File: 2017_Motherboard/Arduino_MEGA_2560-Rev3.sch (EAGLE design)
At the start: 93 parts, among them IC1 NCP1117ST50T3G, IC2 FT232RL, IC3 ATMEGA2560-16AU, IC4 MAX4312ESE, IC5 MAX3468CPA, IC7 LMV358IDGKR, X1 POWERSUPPLY_DC21MMX, Y1 CSTCE16M0V53-R0 16MHZ

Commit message: Updated part names
minor changes
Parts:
- renumbered J9 to ESC_PWM_GND
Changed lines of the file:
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@@
 <part name="J7" library="SparkFun-Connectors" deviceset="M02" device="PTH"/>
 <part name="J8" library="SparkFun-Connectors" deviceset="M02" device="PTH"/>
-<part name="J9" library="SparkFun-Connectors" deviceset="M06" device="LONGPADS"/>
+<part name="ESC_PWM_GND" library="SparkFun-Connectors" deviceset="M06" device="LONGPADS"/>
 <part name="J10" library="SparkFun-Connectors" deviceset="M02" device="PTH"/>
 <part name="J11" library="SparkFun-Connectors" deviceset="M02" device="PTH"/>
@@
 <instance part="J7" gate="G$1" x="337.82" y="114.3" rot="R180"/>
 <instance part="J8" gate="G$1" x="337.82" y="127" rot="R180"/>
-<instance part="J9" gate="G$1" x="261.62" y="38.1" rot="MR0"/>
+<instance part="ESC_PWM_GND" gate="G$1" x="261.62" y="38.1" rot="MR0"/>
 <instance part="J10" gate="G$1" x="152.4" y="-76.2" rot="R180"/>
 <instance part="J11" gate="G$1" x="104.14" y="-48.26" rot="R180"/>
@@
 </segment>
 <segment>
-<pinref part="J9" gate="G$1" pin="6"/>
+<pinref part="ESC_PWM_GND" gate="G$1" pin="6"/>
 <wire x1="256.54" y1="45.72" x2="254" y2="45.72" width="0.1524" layer="91"/>
 <wire x1="254" y1="45.72" x2="254" y2="43.18" width="0.1524" layer="91"/>
-<pinref part="J9" gate="G$1" pin="5"/>
+<pinref part="ESC_PWM_GND" gate="G$1" pin="5"/>
 <wire x1="254" y1="43.18" x2="256.54" y2="43.18" width="0.1524" layer="91"/>
 <wire x1="254" y1="43.18" x2="254" y2="40.64" width="0.1524" layer="91"/>
 <junction x="254" y="43.18"/>
-<pinref part="J9" gate="G$1" pin="4"/>
+<pinref part="ESC_PWM_GND" gate="G$1" pin="4"/>
 <wire x1="254" y1="40.64" x2="256.54" y2="40.64" width="0.1524" layer="91"/>
 <wire x1="254" y1="40.64" x2="254" y2="38.1" width="0.1524" layer="91"/>
 <junction x="254" y="40.64"/>
-<pinref part="J9" gate="G$1" pin="3"/>
+<pinref part="ESC_PWM_GND" gate="G$1" pin="3"/>
 <wire x1="254" y1="38.1" x2="256.54" y2="38.1" width="0.1524" layer="91"/>
 <wire x1="254" y1="38.1" x2="254" y2="35.56" width="0.1524" layer="91"/>
 <junction x="254" y="38.1"/>
-<pinref part="J9" gate="G$1" pin="2"/>
+<pinref part="ESC_PWM_GND" gate="G$1" pin="2"/>
 <wire x1="254" y1="35.56" x2="256.54" y2="35.56" width="0.1524" layer="91"/>
 <wire x1="254" y1="35.56" x2="254" y2="33.02" width="0.1524" layer="91"/>
 <junction x="254" y="35.56"/>
-<pinref part="J9" gate="G$1" pin="1"/>
+<pinref part="ESC_PWM_GND" gate="G$1" pin="1"/>
 <wire x1="254" y1="33.02" x2="256.54" y2="33.02" width="0.1524" layer="91"/>
 <junction x="254" y="33.02"/>

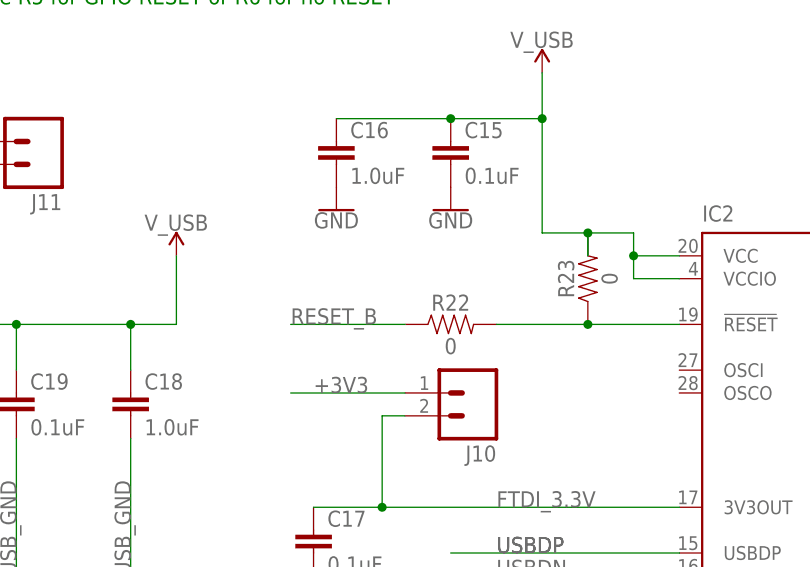
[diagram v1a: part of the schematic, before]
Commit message: Finalized schematic and began layout
FTDI chip is complete, although the AGND on it is a floating pin at the
moment. The RESET_B was changed to RESET on the schematic
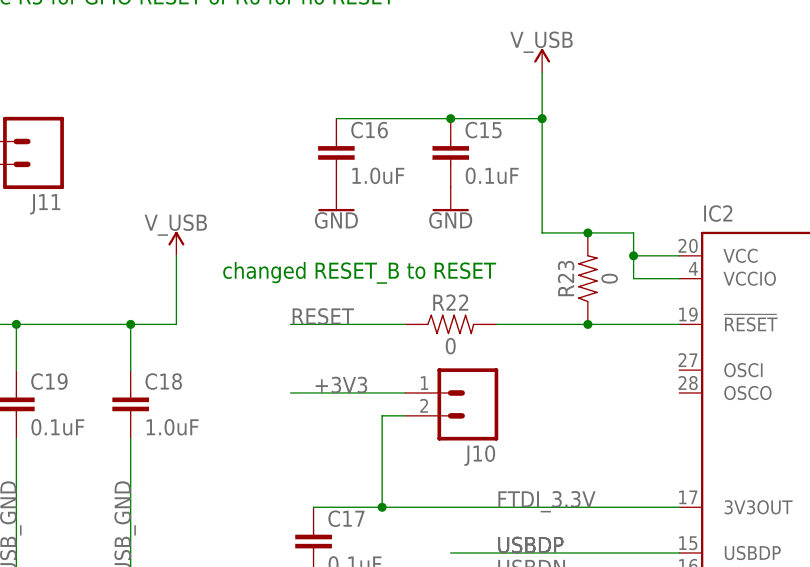
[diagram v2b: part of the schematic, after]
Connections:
- removed net RESET_B: R22.1
- net RESET: now also R22.1
- net V_USB: now also R23.2
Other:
- note added: "changed RESET_B to RESET"
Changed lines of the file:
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@@
 <?xml version="1.0" encoding="utf-8"?>
 <!DOCTYPE eagle SYSTEM "eagle.dtd">
-<eagle version="7.6.0">
+<eagle version="7.7.0">
 <drawing>
 <settings>
@@
 <text x="403.86" y="-68.58" size="1.778" layer="91">Output Transciever</text>
 <text x="444.5" y="-45.72" size="1.778" layer="91">Close these jumpers if no RS485 transciever used</text>
+<text x="124.46" y="-63.5" size="1.778" layer="91">changed RESET_B to RESET</text>
 </plain>
 <instances>
@@
 <junction x="246.38" y="170.18"/>
 </segment>
+<segment>
+<pinref part="R22" gate="G$1" pin="1"/>
+<wire x1="144.78" y1="-68.58" x2="132.08" y2="-68.58" width="0.1524" layer="91"/>
+<label x="132.08" y="-68.58" size="1.778" layer="95"/>
+</segment>
 </net>
 <net name="VIN" class="1">
@@
 <wire x1="160.02" y1="-40.64" x2="160.02" y2="-45.72" width="0.1524" layer="91"/>
 <junction x="160.02" y="-45.72"/>
-<wire x1="165.1" y1="-58.42" x2="165.1" y2="-60.96" width="0.1524" layer="91"/>
-<junction x="165.1" y="-58.42"/>
 <pinref part="IC2" gate="1" pin="VCC"/>
 <wire x1="175.26" y1="-60.96" x2="170.18" y2="-60.96" width="0.1524" layer="91"/>
 <junction x="170.18" y="-60.96"/>
+<pinref part="R23" gate="G$1" pin="2"/>
+<junction x="165.1" y="-58.42"/>
 </segment>
 <segment>
@@
 </segment>
 </net>
-<net name="RESET_B" class="0">
-<segment>
-<pinref part="R22" gate="G$1" pin="1"/>
-<wire x1="144.78" y1="-68.58" x2="132.08" y2="-68.58" width="0.1524" layer="91"/>
-<label x="132.08" y="-68.58" size="1.778" layer="95"/>
-</segment>
-</net>
